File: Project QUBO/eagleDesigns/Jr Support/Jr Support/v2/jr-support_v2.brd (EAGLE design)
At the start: 242.6 x 96.8 mm, 250 parts, among them IC1 74LVC1G08DBV, IC2 TLC2272PW, IC3 74LVC1G08DBV, IC4 74LVC1G08DBV, Q1 FDN5618P, U1 PCA9685, U2 LT3063, U3 LT3063

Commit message: 
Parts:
- removed LED3: Green, led:CHIP-LED0805
- removed R28: 50k, resistor:R0805
- added 5V_PG: (no value), led:CHIP-LED0805
- added FAULT2: (no value), pinhead:1X02
- added ON_INDICATOR: Green, led:CHIP-LED0805
- added R2: 1.2k, resistor:R0805
- added R3: 50k, resistor:R0805
- added U$1: DMP32D5SFB, transistor-fet:AP02002
- moved R61 256.7 mm to (-8.13, 51.8)
- moved R1 250.4 mm to (74.2, 20.1), turned to 90 degrees
- moved FAULT1 247.2 mm to (-2.79, 51.8)
- moved R25 245.2 mm to (110.2, 108.5)
- moved C53 241.8 mm to (80.0, 37.6), turned to 270 degrees
- moved U$50 239.3 mm to (99.6, 133.3)
- moved R60 236.6 mm to (-8.13, 54.6)
- moved C1 236.0 mm to (101.9, 108.5)
- moved C70 231.6 mm to (-7.24, 76.8)
- moved FAULT1_DISABLE 231.6 mm to (-2.79, 47.0), turned to 90 degrees
- moved R33 230.4 mm to (103.1, 113.0)
- moved C75 230.2 mm to (-1.14, 65.2), turned to 270 degrees
- moved 5V_LED 227.6 mm to (74.9, -19.1), turned to 270 degrees
- moved U2 221.8 mm to (-7.87, 73.7), turned to 270 degrees
- moved C72 221.3 mm to (-2.03, 74.9), turned to 270 degrees
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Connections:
- new net N$3: FAULT2.1, IC4.2, R61.1
- new net N$4: 5V_PG.A, R2.1
- new net N$5: R2.2, U$1.P$3
- new net N$6: 5V_REG.19, R3.1, U$1.P$2
- net 5V_PG: now also FAULT2.2; no longer 5V_REG.19, IC4.2, R28.1, R61.1
- net GND: now also 5V_PG.C, ON_INDICATOR.C; no longer LED3.C
- net N$84: now also ON_INDICATOR.A; no longer LED3.A
- net RELAY_OUT: now also R3.2, U$1.P$1; no longer R28.2
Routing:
- net T4_CURR: track 20.6 -> 0.00 mm, vias 1 -> 0
- net T3_CURR: track 17.7 -> 0.00 mm, vias 1 -> 0
- net 5V: track 39.4 -> 32.8 mm, vias 8 -> 5
- net T8_CURR: track 2.54 -> 0.00 mm, vias 1 -> 0
- net GND: track 46.1 -> 44.7 mm, vias 24 -> 23
- net N$63: track 0.00 -> 0.71 mm
- added copper zone on layer 1, net N$17
- removed copper zone on layer 1, net 17
- removed copper zone on layer 16, net 5V
- removed copper zone on layer 1, net N$15
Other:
- board size 242.6 x 96.8 mm -> 204.5 x 127 mm

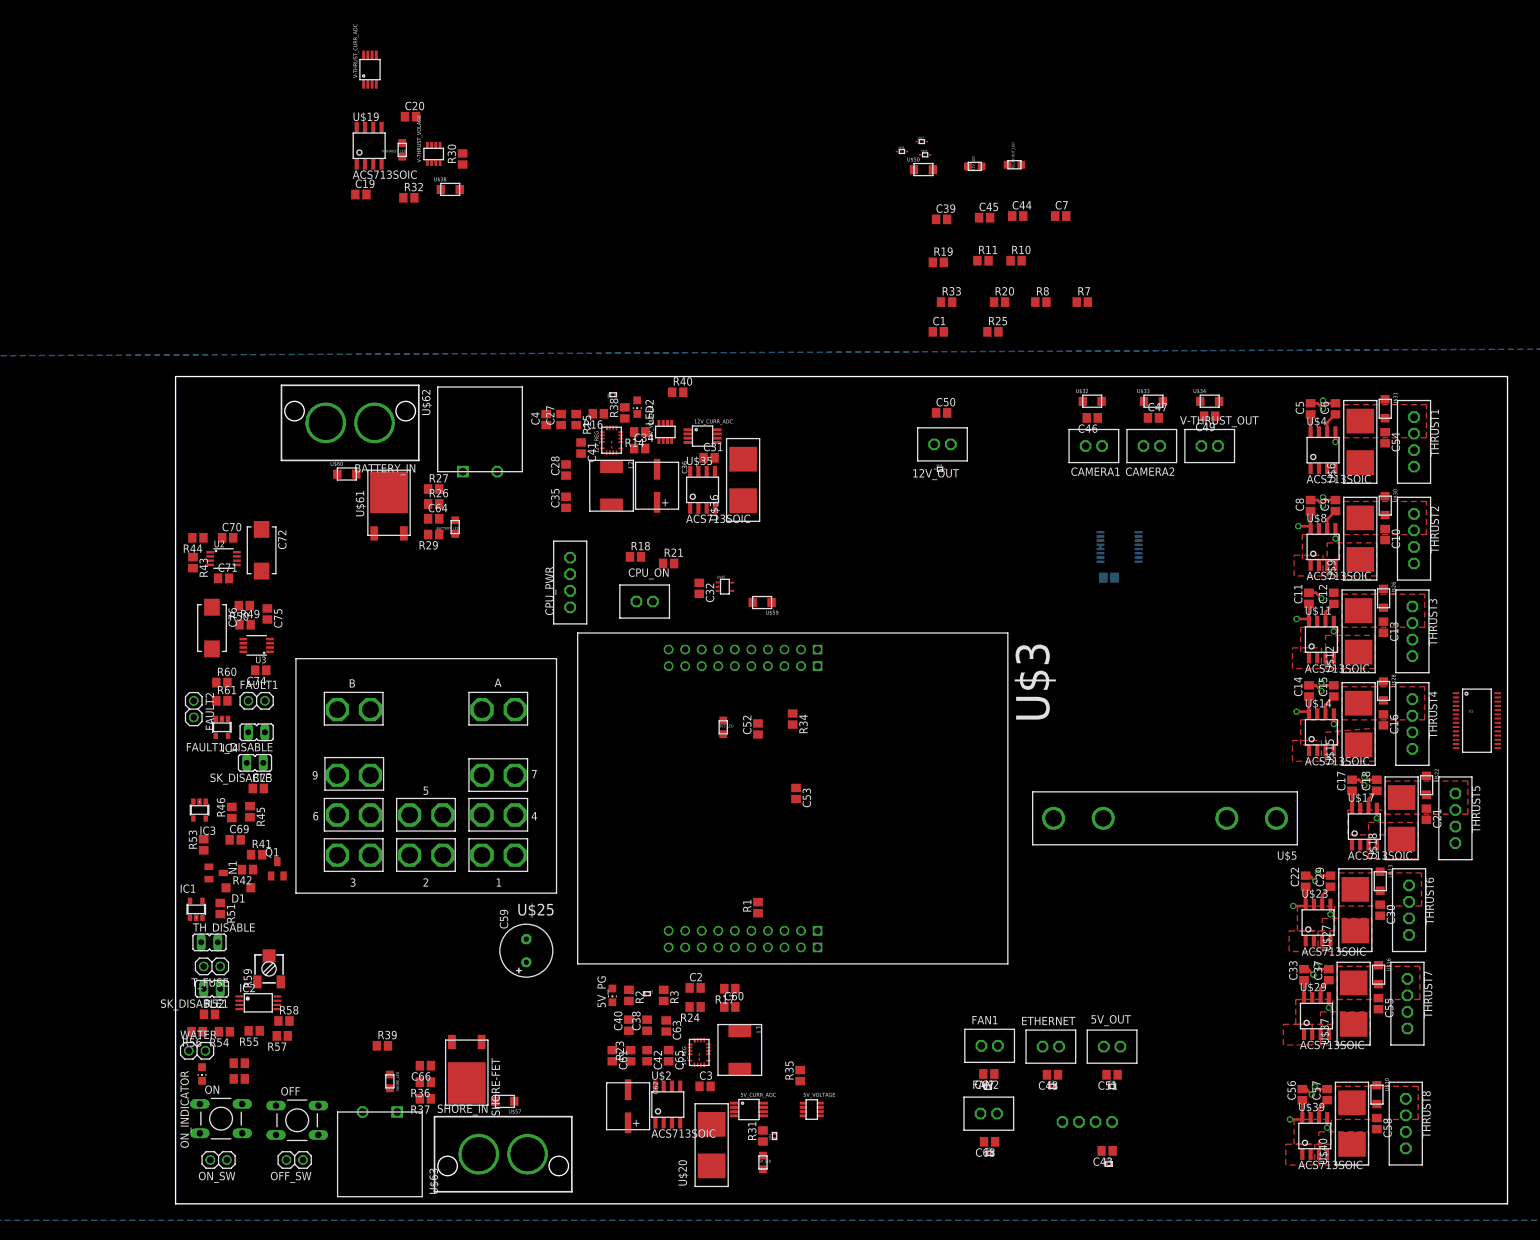
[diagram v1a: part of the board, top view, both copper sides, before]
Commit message: 
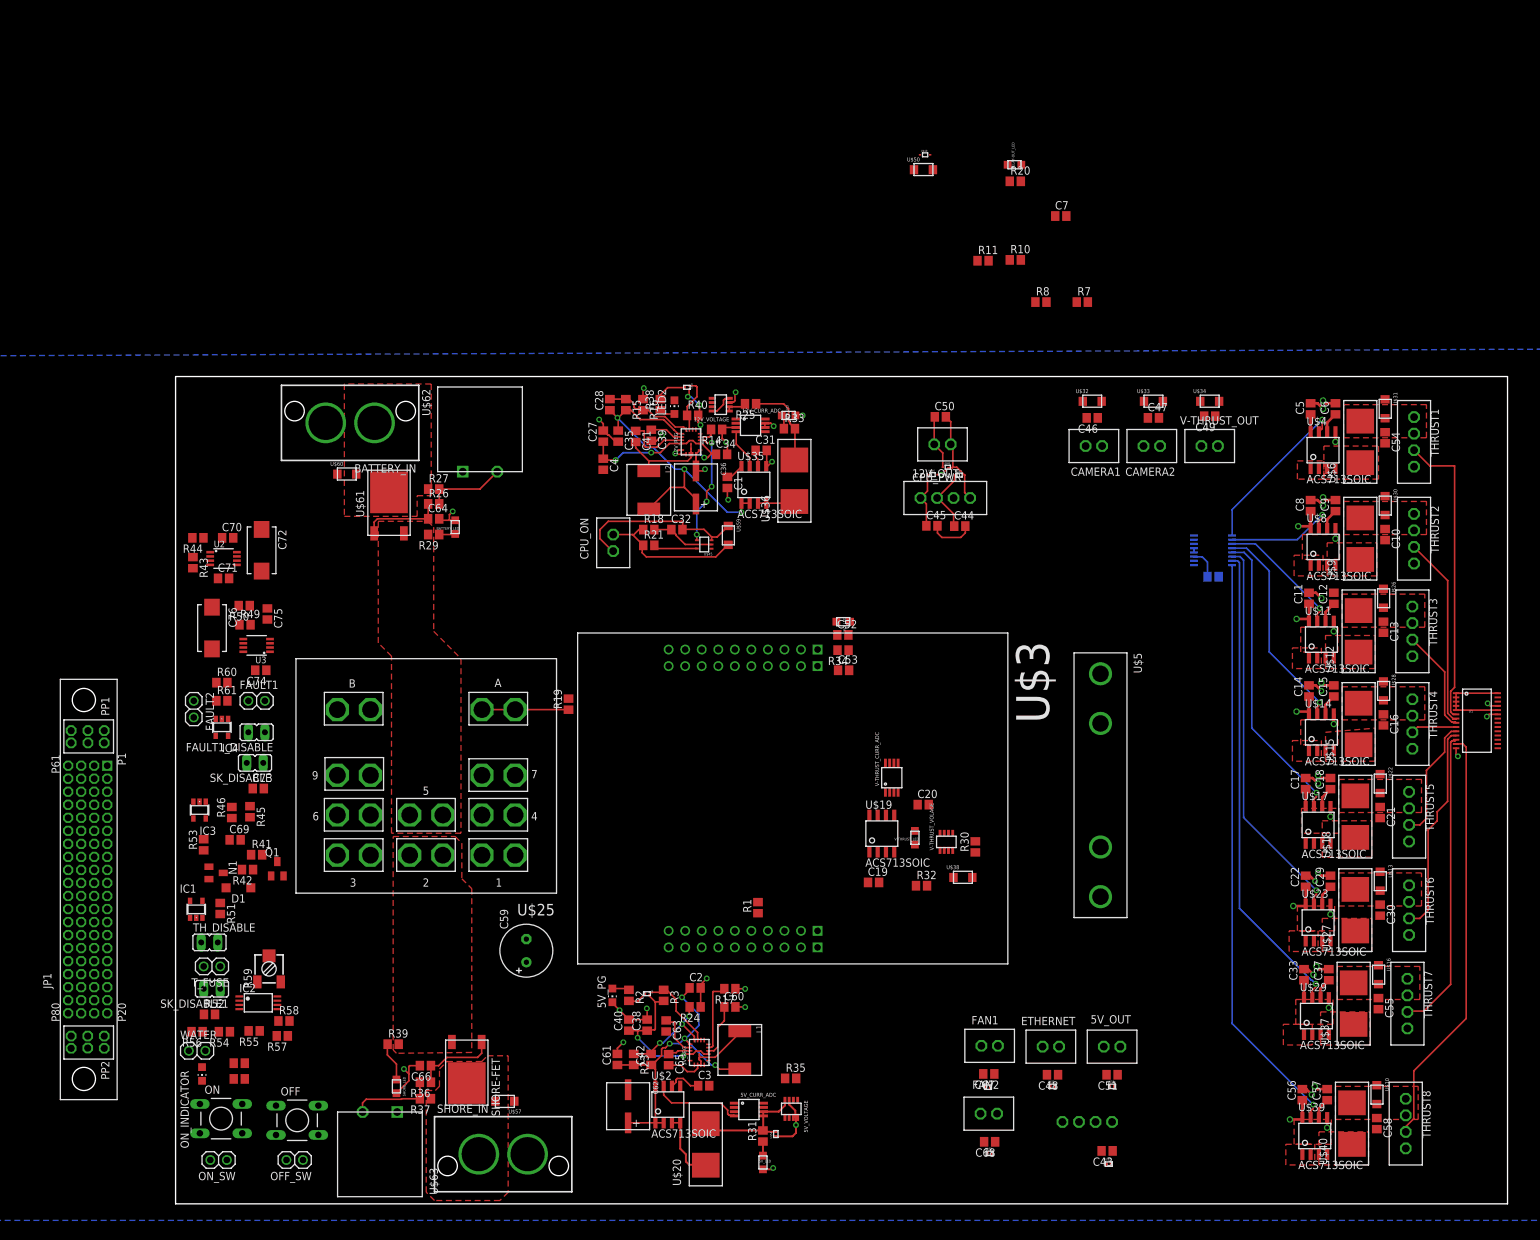
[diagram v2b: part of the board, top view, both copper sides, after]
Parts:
- added JP1: (no value), samtec:MPSC-01-80
- moved V-THRUST_CURR_ADC 135.0 mm to (94.7, 40.0)
- moved C19 131.7 mm to (91.9, 23.9)
- moved C20 131.7 mm to (99.5, 35.9)
- moved R30 131.7 mm to (107.5, 29.4)
- moved R32 131.7 mm to (99.3, 23.4)
- moved U$19 131.7 mm to (93.2, 31.4)
- moved U$38 131.7 mm to (105.6, 24.7)
- moved V-THRUST_LED 131.7 mm to (98.3, 30.8)
- moved V-THRUST_VOLAGE 131.7 mm to (103.1, 30.2)
- moved R19 88.4 mm to (45.1, 51.3), turned to 90 degrees
- moved CPU_PWR 59.0 mm to (102.9, 83.0), turned to 0 degrees
- moved C39 55.6 mm to (57.8, 92.6), turned to 270 degrees
- moved U$47 51.5 mm to (105.1, 86.5)
- moved U$46 49.8 mm to (101.0, 86.5)
- moved C44 48.4 mm to (105.1, 78.6)
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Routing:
- net GND: track 44.7 -> 152.2 mm, vias 23 -> 48
- net T8_CURR: track 0.00 -> 90.2 mm, vias 0 -> 1
- net T7_CURR: track 0.00 -> 73.2 mm, vias 0 -> 1
- net RELAY_OUT: track 0.50 -> 69.1 mm, vias 0 -> 8
- net T8_PWM: track 0.00 -> 64.7 mm
- net T6_CURR: track 0.00 -> 59.6 mm, vias 0 -> 1
- net N$7: track 0.00 -> 56.1 mm, vias 0 -> 3
- net SW-5V: track 0.00 -> 49.5 mm, vias 0 -> 4
- net 5V: track 32.8 -> 80.2 mm
- net T7_PWM: track 0.00 -> 46.6 mm
- net T1_PWM: track 0.00 -> 46.2 mm
- net T5_CURR: track 0.00 -> 45.6 mm, vias 0 -> 1
- net 12V: track 0.00 -> 41.1 mm
- net T4_CURR: track 0.00 -> 32.8 mm, vias 0 -> 1
- net T6_PWM: track 0.00 -> 32.5 mm
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- added copper zone on layer 1, net N$15
- added copper zone on layer 1, net N$50
- added copper zone on layer 1, net N$64
- added copper zone on layer 1, net N$9
- added copper zone on layer 1, net RELAY-BATT

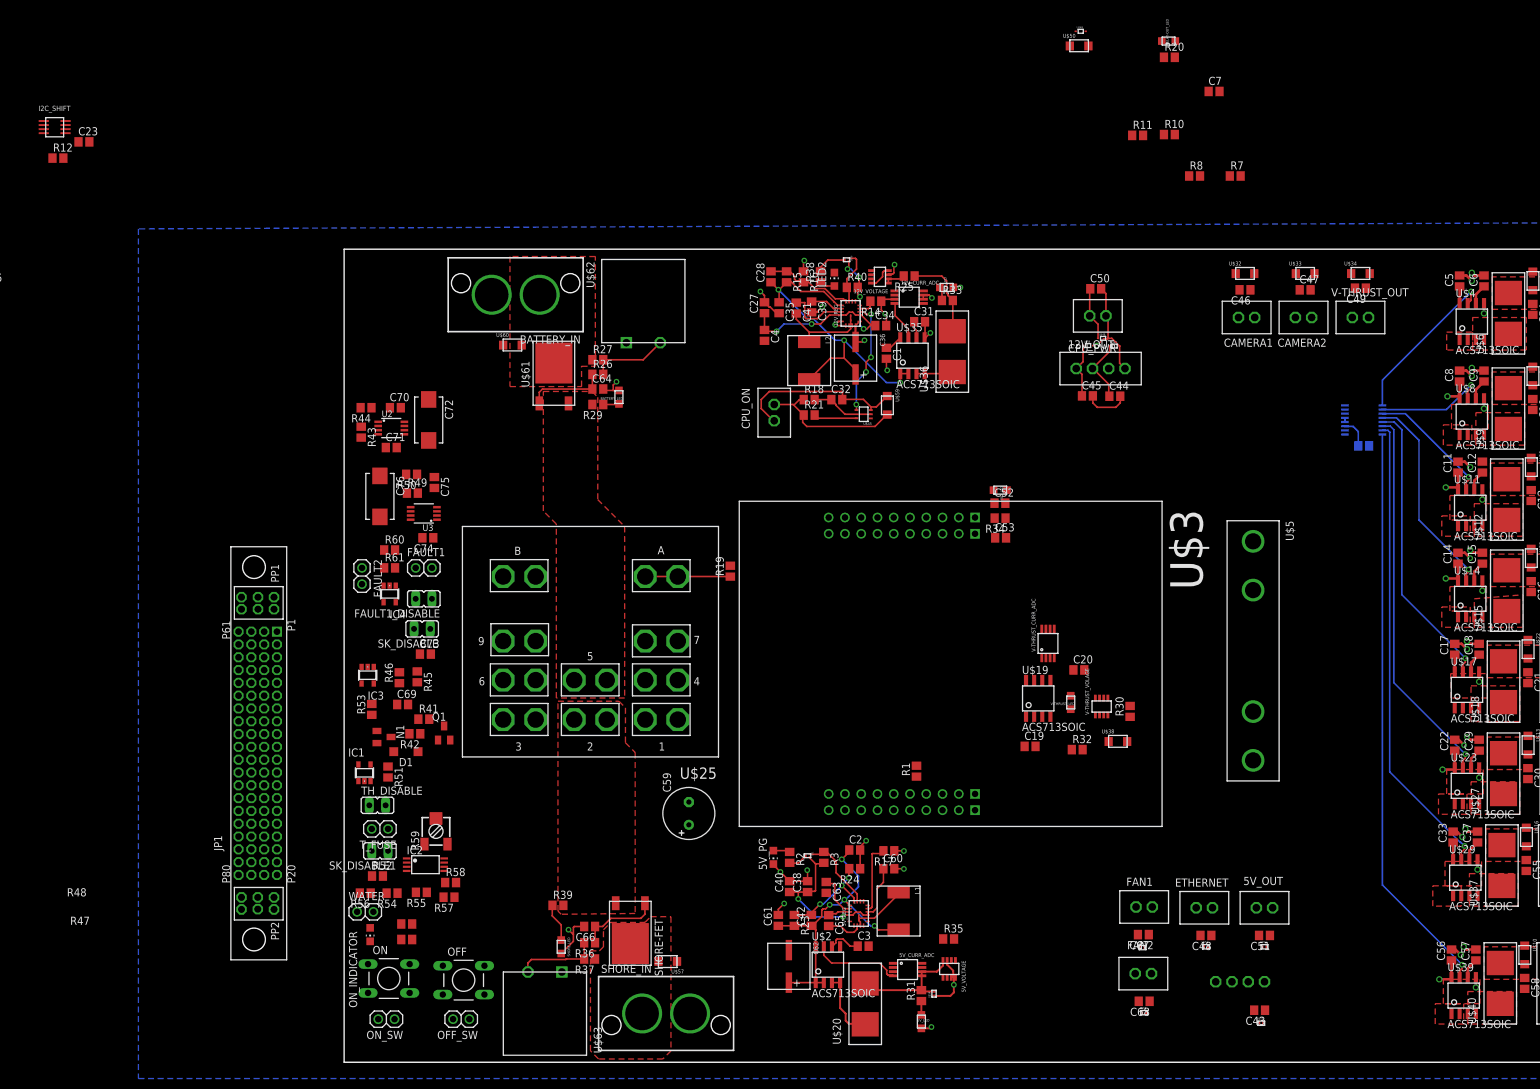
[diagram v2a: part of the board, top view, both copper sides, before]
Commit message: 
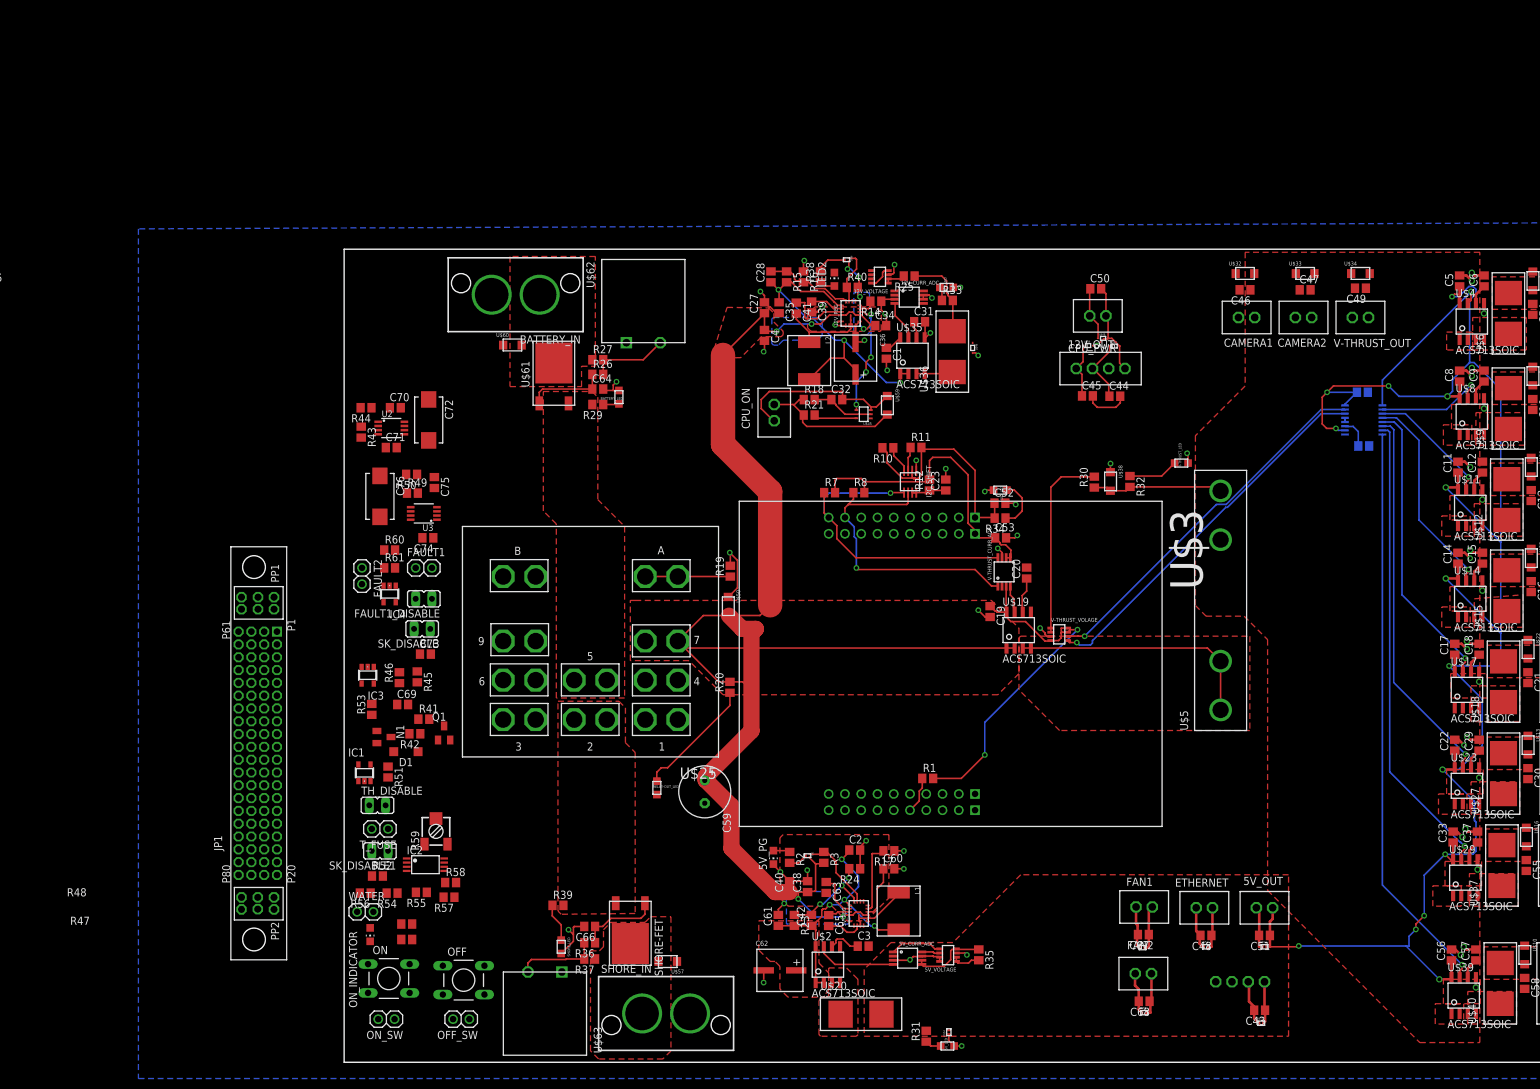
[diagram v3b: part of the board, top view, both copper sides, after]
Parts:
- moved R12 145.4 mm to (76.2, 64.8), turned to 90 degrees
- moved C23 144.9 mm to (78.7, 64.8), turned to 90 degrees
- moved I2C_SHIFT 144.6 mm to (73.2, 65.3), turned to 180 degrees
- moved RELAY-OUT_LED 141.4 mm to (33.6, 17.5), turned to 270 degrees
- moved R20 120.0 mm to (45.0, 33.2), turned to 90 degrees
- moved U$50 103.3 mm to (44.8, 45.8), turned to 270 degrees
- moved R7 80.4 mm to (60.6, 63.6)
- moved R8 72.1 mm to (65.2, 63.6)
- moved R10 65.8 mm to (69.7, 70.6), turned to 180 degrees
- moved R11 59.8 mm to (74.1, 70.6)
- moved C7 52.4 mm to (143.8, 79.3), flipped to the bottom, turned to 180 degrees
- moved U$49 52.3 mm to (82.9, 86.2), turned to 270 degrees
- moved R32 42.7 mm to (107.5, 65.3), turned to 270 degrees
- moved V-THRUST_LED 41.2 mm to (115.5, 68.2), turned to 0 degrees
- moved U$38 40.6 mm to (104.5, 65.3), turned to 270 degrees
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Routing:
- net 5V: track 80.2 -> 447.6 mm, vias 5 -> 16
- net RELAY_OUT: track 69.1 -> 302.2 mm
- net SCL1: track 0.00 -> 114.3 mm, vias 0 -> 2
- net SDA1: track 0.00 -> 111.5 mm, vias 0 -> 2
- net GND: track 152.2 -> 221.5 mm, vias 48 -> 63
- net N$34: track 0.00 -> 39.4 mm
- net 3V3: track 0.00 -> 38.1 mm
- net N$58: track 0.00 -> 30.1 mm
- net V_THRUST: track 0.00 -> 20.4 mm
- net N$68: track 0.00 -> 19.2 mm
- net N$55: track 10.9 -> 1.27 mm
- net N$74: track 0.00 -> 8.02 mm
- net N$72: track 0.00 -> 7.81 mm
- net N$41: track 0.00 -> 6.02 mm
- net N$2: track 0.00 -> 5.76 mm
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- added copper zone on layer 1, net 5V
- added copper zone on layer 1, net N$34
- added copper zone on layer 1, net N$55
- added copper zone on layer 1, net RELAY-SHORE
- added copper zone on layer 1, net RELAY_OUT
- added copper zone on layer 16, net RELAY_OUT
- added copper zone on layer 1, net SW-5V
- removed copper zone on layer 1, net N$9

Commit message: 
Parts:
- moved C24 163.0 mm to (66.6, 22.2)
- moved BME280 156.3 mm to (62.6, 23.3), turned to 90 degrees
- moved C25 156.0 mm to (66.5, 24.7)
- moved C26 146.7 mm to (58.0, 25.4), turned to 180 degrees
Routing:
- net GND: track 221.5 -> 247.7 mm, vias 63 -> 66
- net 3V3: track 38.1 -> 52.0 mm
- net SDA-3V3: track 4.28 -> 7.67 mm, vias 0 -> 1

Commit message: 
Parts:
- moved R52 23.9 mm to (8.18, 19.1), turned to 270 degrees
- moved R54 20.8 mm to (8.13, 14.5), turned to 270 degrees
- moved R56 17.5 mm to (2.77, 10.5)
- moved R55 14.4 mm to (8.23, 9.88), turned to 90 degrees
- moved R53 11.9 mm to (-9.19, 41.5), turned to 270 degrees
- moved R59 11.5 mm to (-1.45, 22.2), turned to 90 degrees
- moved IC2 10.8 mm to (-1.40, 16.2)
- moved R58 10.7 mm to (2.72, 13.3), turned to 180 degrees
- moved N1 8.66 mm to (-8.10, 34.0)
- moved IC3 8.65 mm to (-5.92, 41.6)
- moved Q1 8.47 mm to (0.84, 34.5)
- moved R42 8.22 mm to (-3.12, 34.1)
- moved FAULT2 7.89 mm to (-11.9, 58.4), turned to 90 degrees
- moved R46 7.71 mm to (-1.19, 40.2)
- moved D1 7.55 mm to (-5.21, 30.7)
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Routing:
- net +5V: track 0.00 -> 122.0 mm, vias 0 -> 3
- net SDA1: track 111.5 -> 228.7 mm, vias 2 -> 3
- net SCL1: track 114.3 -> 230.9 mm, vias 2 -> 5
- net VDD: track 0.00 -> 113.9 mm, vias 0 -> 3
- net FAULT: track 0.00 -> 90.0 mm, vias 0 -> 3
- net ON_SW: track 0.00 -> 60.3 mm, vias 0 -> 1
- net GND: track 247.7 -> 287.3 mm, vias 66 -> 70
- net RELAY-CTRL: track 0.00 -> 30.1 mm
- net VCC: track 0.00 -> 27.2 mm, vias 0 -> 2
- net RELAY-BATT: track 0.00 -> 24.5 mm
- net 5V: track 447.6 -> 468.9 mm, vias 16 -> 18
- net WATER: track 0.00 -> 16.5 mm
- net N$88: track 0.00 -> 13.9 mm
- net N$87: track 0.00 -> 13.8 mm
- net N$76: track 0.00 -> 13.4 mm
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- added copper zone on layer 1, net 12V

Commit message: 
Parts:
- moved FAULT1 0.55 mm to (-0.51, 54.3)
- moved R57 0.15 mm to (3.28, 7.62)
- moved C47 0.08 mm to (134.9, 95.2), turned to 180 degrees
- moved U$33 0.08 mm to (134.9, 97.7)
- renumbered V-THRUST_VOLAGE to V-THRUST_VOLTAGE
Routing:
- net GND: track 287.3 -> 494.1 mm, vias 70 -> 90
- net SDA-3V3: track 7.67 -> 159.0 mm, vias 1 -> 4
- net SCL1: track 230.9 -> 378.5 mm, vias 5 -> 11
- net SCL-3V3: track 3.81 -> 143.1 mm, vias 0 -> 4
- net SDA1: track 228.7 -> 363.2 mm, vias 3 -> 9
- net 5V: track 468.9 -> 544.3 mm, vias 18 -> 24
- net 3V3: track 52.0 -> 99.5 mm, vias 0 -> 1
- net +5V: track 122.0 -> 122.9 mm
- net N$76: track 13.4 -> 14.0 mm
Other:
- board text added: "Tiva Debugger Side"

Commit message: 
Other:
- board size 204.5 x 127 mm -> 205.7 x 127 mm
